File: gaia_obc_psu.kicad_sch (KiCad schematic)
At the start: 20 parts, among them J3 Conn_01x02_Pin, Q1 FS8205A, U2 LGS4056H, U3 DW01A, U5 AP2112K-3.3, U8 INA219AxDCN

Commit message: preparing ina3221
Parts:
- removed J3: Conn_01x02_Pin, Connector_Molex:Molex_MicroClasp_55935-0230_1x02_P2.00mm_Horizontal, symbol Connector:Conn_01x02_Pin
- removed U8: INA219AxDCN, Package_TO_SOT_SMD:SOT-23-8, symbol Sensor_Energy:INA219AxDCN
- added J4: Conn_01x02_Pin, Connector_Molex:Molex_MicroClasp_55935-0230_1x02_P2.00mm_Horizontal, symbol Connector:Conn_01x02_Pin
- added R13, R14, R15, R16, R17, R18: R_Small, symbol Device:R_Small
- added R19, R20, R21, R22: 10k, symbol Device:R_Small
- added U10, U9: INA3221, Package_DFN_QFN:Texas_RGV0016A_VQFN-16-1EP_4x4mm_P0.65mm_EP2.1x2.1mm, symbol Power_Management:INA3221
- added U11, U12, U8: AP2112K-3.3, Package_TO_SOT_SMD:SOT-23-5, symbol Regulator_Linear:AP2112K-3.3
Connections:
- net +BATT: now also J4.1 (Pin_1)
- net GND: now also U11.2 (GND), U12.2 (GND), U8.2 (GND), U9.17 (EP), U9.3 (GND)
- net VCC: now also J4.2 (Pin_2), R13.1, R14.1, R15.1, U9.1 (IN-3), U9.11 (IN-1), U9.14 (IN-2), U9.4 (VS), U9.5 (A0); no longer C9.1, U5.1 (VIN), U5.3 (EN)
- new net: R19.2, U9.9 (CRITICAL)
- new net: R22.2, U9.10 (PV)
- new net: R15.2, U9.12 (IN+1)
- new net: R21.2, U9.13 (TC)
- new net: R14.2, U9.15 (IN+2)
- new net: R22.1, U9.16 (VPU)
- new net: R13.2, U9.2 (IN+3)
- new net: R20.2, U9.8 (WARNING)
- new net: C9.1, U5.1 (VIN), U5.3 (EN)
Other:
- moved on the sheet: C7, C8, C9, U5

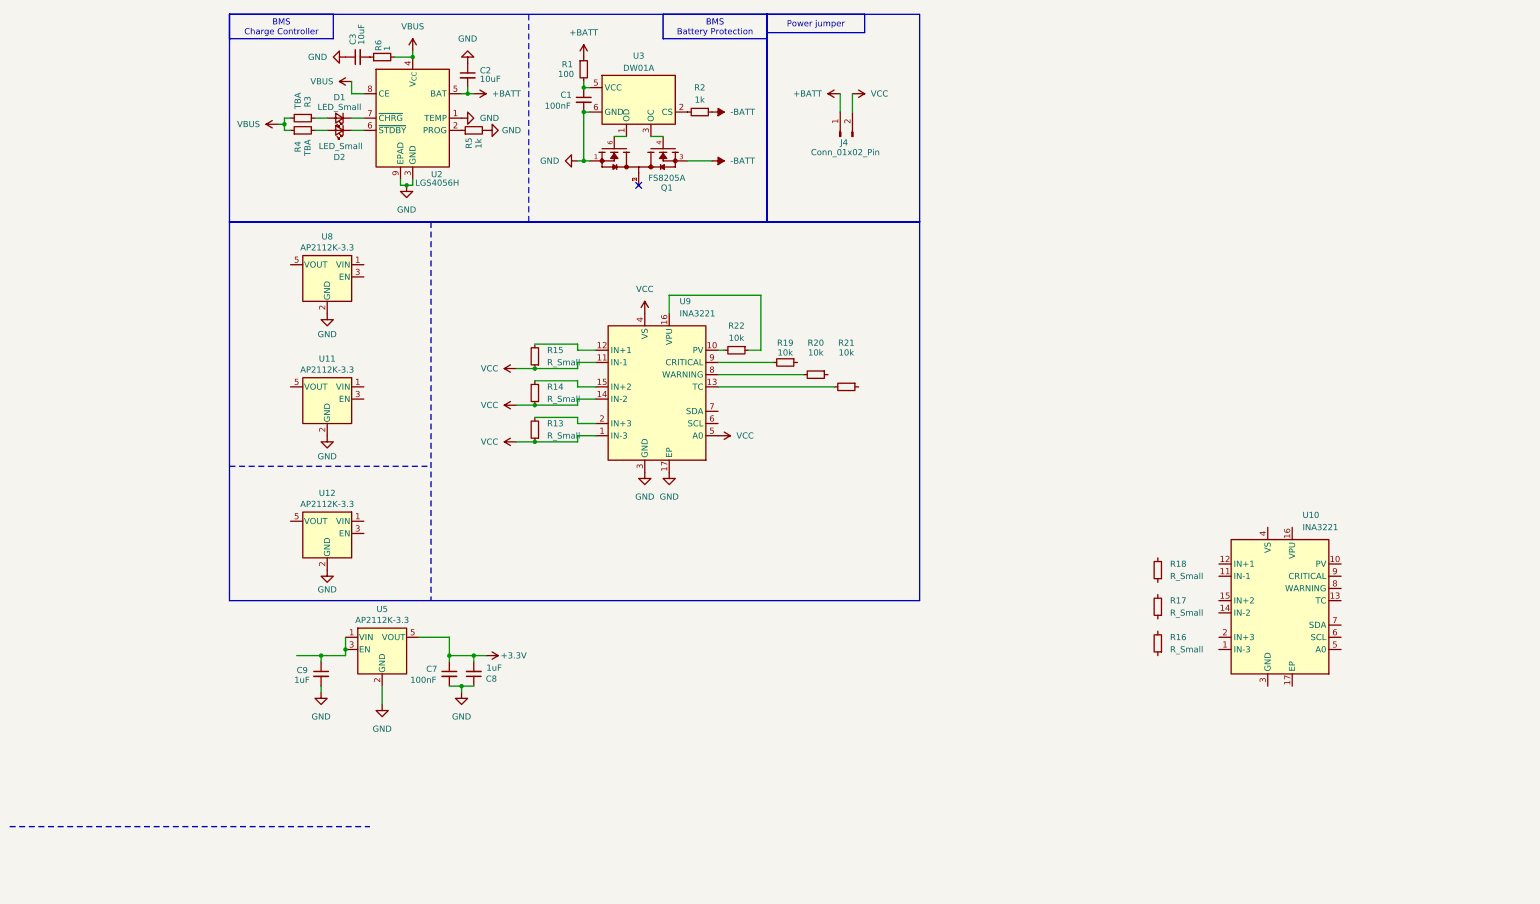
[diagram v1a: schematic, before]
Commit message: creating psu switches
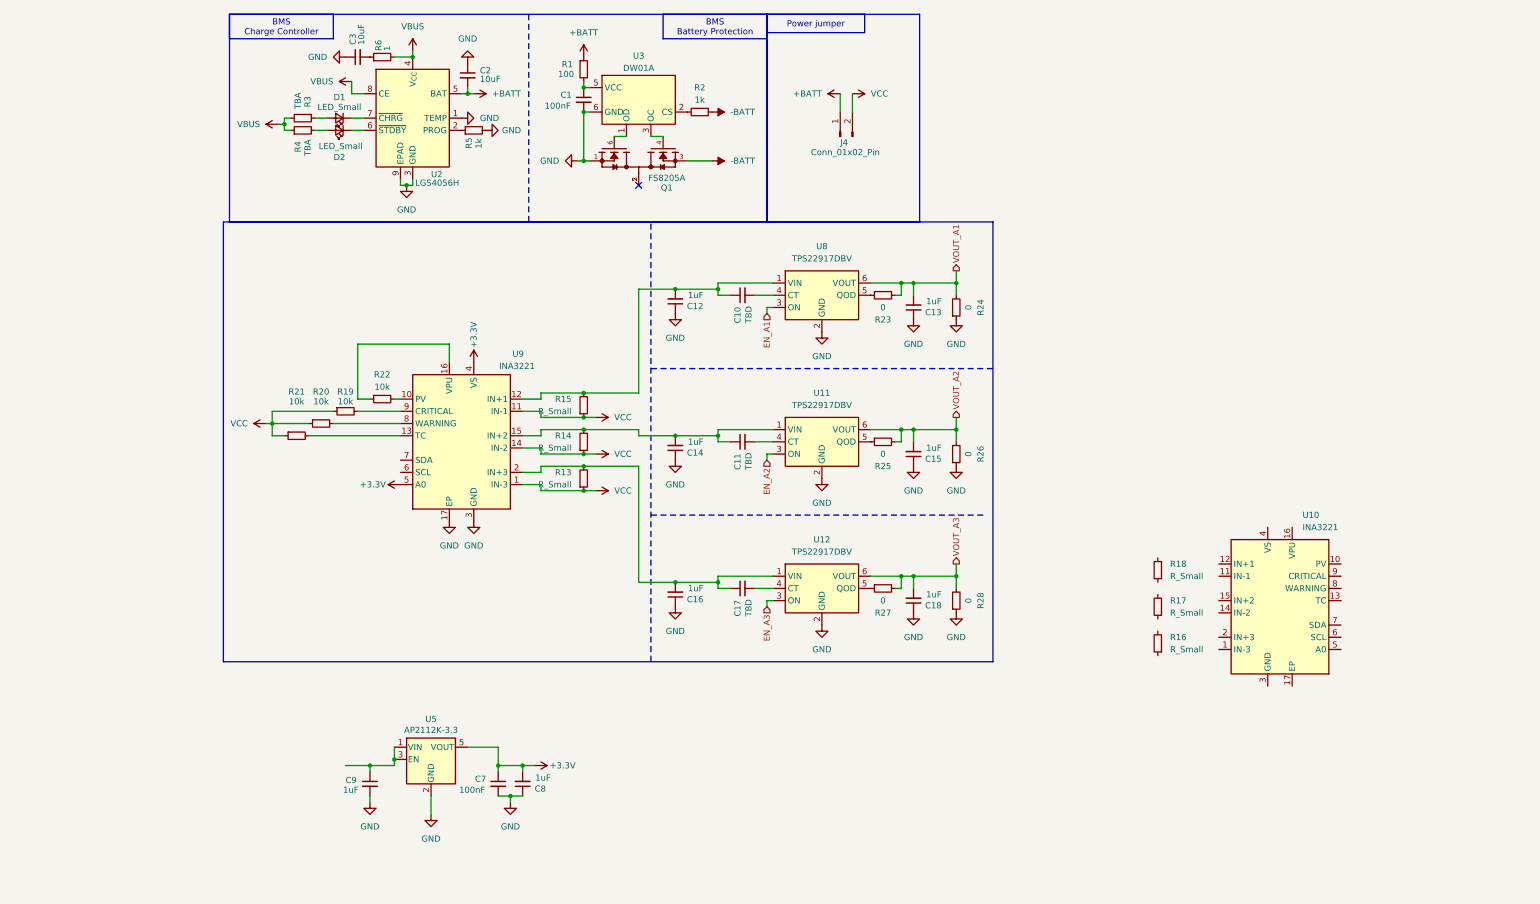
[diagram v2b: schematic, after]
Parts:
- removed U11, U12, U8: AP2112K-3.3, Package_TO_SOT_SMD:SOT-23-5, symbol Regulator_Linear:AP2112K-3.3
- added C10, C11, C17: TBD, symbol Device:C_Small
- added C12, C13, C14, C15, C16, C18: 1uF, symbol Device:C_Small
- added R23, R24, R25, R26, R27, R28: 0, symbol Device:R_Small
- added U11, U12, U8: TPS22917DBV, Package_TO_SOT_SMD:SOT-23-6, symbol Power_Management:TPS22917DBV
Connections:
- net +3.3V: now also U9.4 (VS), U9.5 (A0)
- net GND: now also C12.1, C13.1, C14.1, C15.1, C16.1, C18.1, R24.1, R26.1, R28.1, U11.2 (GND), U12.2 (GND), U8.2 (GND)
- net VCC: now also R19.1, R20.1, R21.1; no longer U9.4 (VS), U9.5 (A0)
- net at R15.2, U9.12 (IN+1): now also C10.1, C12.2, U8.1 (VIN)
- net at R14.2, U9.15 (IN+2): now also C11.1, C14.2, U11.1 (VIN)
- net at R13.2, U9.2 (IN+3): now also C16.2, C17.1, U12.1 (VIN)
- new net: C10.2, U8.4 (CT)
- new net: C11.2, U11.4 (CT)
- new net: R25.1, U11.5 (QOD)
- new net: R23.1, U8.5 (QOD)
- new net: C17.2, U12.4 (CT)
- new net: R27.1, U12.5 (QOD)
- new net EN_A1: U8.3 (ON)
- new net EN_A2: U11.3 (ON)
- new net EN_A3: U12.3 (ON)
- new net VOUT_A1: C13.2, R23.2, R24.2, U8.6 (VOUT)
- new net VOUT_A2: C15.2, R25.2, R26.2, U11.6 (VOUT)
- new net VOUT_A3: C18.2, R27.2, R28.2, U12.6 (VOUT)
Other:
- moved on the sheet: C7, C8, C9, R13, R14, R15, R19, R20, R21, R22, U5, U9

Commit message: finishing psu
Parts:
- removed R16, R17, R18: R_Small, symbol Device:R_Small
- removed U10: INA3221, Package_DFN_QFN:Texas_RGV0016A_VQFN-16-1EP_4x4mm_P0.65mm_EP2.1x2.1mm, symbol Power_Management:INA3221
- removed U2: LGS4056H, Package_DFN_QFN:DFN-8-1EP_3x3mm_P0.65mm_EP1.7x2.05mm, symbol OnionSAT_Gaia:LGS4056H
- added C19, C20, C25, C26: 1uF, symbol Device:C_Small
- added C22, C23: TBD, symbol Device:C_Small
- added R29, R30, R31, R32: 10k, symbol Device:R_Small
- added R33, R34, R35: R_Small, symbol Device:R_Small
- added R36, R37, R39, R40: 0, symbol Device:R_Small
- added U10: TP4056-42-ESOP8, Package_SO:SOIC-8-1EP_3.9x4.9mm_P1.27mm_EP2.41x3.3mm_ThermalVias, symbol Battery_Management:TP4056-42-ESOP8
- added U13: INA3221, Package_DFN_QFN:Texas_RGV0016A_VQFN-16-1EP_4x4mm_P0.65mm_EP2.1x2.1mm, symbol Power_Management:INA3221
- added U14, U15: TPS22917DBV, Package_TO_SOT_SMD:SOT-23-6, symbol Power_Management:TPS22917DBV
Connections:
- net +3.3V: now also R19.1, R20.1, R21.1, R29.1, R30.1, R31.1, U13.4 (VS), U13.5 (A0)
- net +BATT: now also U10.5 (BAT)
- net EN_A1: now also U14.3 (ON)
- net EN_A2: now also U15.3 (ON)
- net GND: now also C19.1, C20.1, C25.1, C26.1, R39.1, R40.1, U10.1 (TEMP), U10.3 (GND), U10.9 (EPAD), U13.17 (EP), U13.3 (GND), U14.2 (GND), U15.2 (GND)
- net VBUS: now also U10.4 (V_{CC}), U10.8 (CE)
- net VCC: now also R33.1, R34.1, R35.1, U13.1 (IN-3), U13.11 (IN-1), U13.14 (IN-2); no longer R19.1, R20.1, R21.1
- net VOUT_A1: now also C25.2, R36.2, R39.2, U14.6 (VOUT)
- net VOUT_A2: now also C26.2, R37.2, R40.2, U15.6 (VOUT)
- net at R5.1: now also U10.2 (PROG)
- net at D2.1 (K): now also U10.6 (~{STDBY})
- net at D1.1 (K): now also U10.7 (~{CHRG})
- net at C9.1, U5.1 (VIN), U5.3 (EN): now also R35.2, U13.2 (IN+3)
- new net: C19.2, C22.1, R33.2, U13.12 (IN+1), U14.1 (VIN)
- new net: R30.2, U13.8 (WARNING)
- new net: C20.2, C23.1, R34.2, U13.15 (IN+2), U15.1 (VIN)
- new net: C23.2, U15.4 (CT)
- new net: R37.1, U15.5 (QOD)
- new net: C22.2, U14.4 (CT)
- new net: R29.2, U13.13 (TC)
- new net: R32.2, U13.10 (PV)
- new net: R32.1, U13.16 (VPU)
- new net: R31.2, U13.9 (CRITICAL)
- new net: R36.1, U14.5 (QOD)
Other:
- moved on the sheet: C1, C10, C11, C12, C13, C14, C15, C16, C17, C18, C2, C3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

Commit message: almost final release
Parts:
- removed U10: TP4056-42-ESOP8, Package_SO:SOIC-8-1EP_3.9x4.9mm_P1.27mm_EP2.41x3.3mm_ThermalVias, symbol Battery_Management:TP4056-42-ESOP8
- added C32: 10uF, Capacitor_SMD:C_0402_1005Metric, symbol Device:C_Small
- added C33, C37: 1uF, Capacitor_SMD:C_0402_1005Metric, symbol Device:C_Small
- added C35: 100nF, Capacitor_SMD:C_0402_1005Metric, symbol Device:C_Small
- added IC1: MAX17048G+T10, gaia_obc-footprints:SON50P200X200X80-9N-D, symbol gaia_obc-symbols:MAX17048G+T10
- added R44, R45: 100k, symbol Device:R_Small
- added U13: AP2112K-3.0, Package_TO_SOT_SMD:SOT-23-5, symbol Regulator_Linear:AP2112K-3.3
- added U14: LGS4056HDB, Package_DFN_QFN:DFN-8-1EP_3x3mm_P0.65mm_EP1.55x2.4mm, symbol gaia_obc-symbols:LGS4056HDB
- C13: renamed from C12; footprint (none) -> Capacitor_SMD:C_0402_1005Metric
- C14: footprint (none) -> Capacitor_SMD:C_0402_1005Metric
- C15: renamed from C16; footprint (none) -> Capacitor_SMD:C_0402_1005Metric
- C16: renamed from C19; footprint (none) -> Capacitor_SMD:C_0402_1005Metric
- C17: renamed from C20; footprint (none) -> Capacitor_SMD:C_0402_1005Metric
- C18: renamed from C10; value TBD -> 1nF
- C19: renamed from C11; value TBD -> 1nF
- C20: renamed from C17; value TBD -> 1nF
- C21: renamed from C22; value TBD -> 1nF
- C22: renamed from C23; value TBD -> 1nF
- C23: renamed from C9; footprint (none) -> Capacitor_SMD:C_0402_1005Metric
- C24: renamed from C7; footprint (none) -> Capacitor_SMD:C_0402_1005Metric
- C25: renamed from C8; footprint (none) -> Capacitor_SMD:C_0402_1005Metric
- C26: renamed from C13; footprint (none) -> Capacitor_SMD:C_0402_1005Metric
- C27: renamed from C15; footprint (none) -> Capacitor_SMD:C_0402_1005Metric
- C28: renamed from C18; footprint (none) -> Capacitor_SMD:C_0402_1005Metric
- C29: renamed from C25; footprint (none) -> Capacitor_SMD:C_0402_1005Metric
- C30: renamed from C26; footprint (none) -> Capacitor_SMD:C_0402_1005Metric
- C31: renamed from C1; footprint (none) -> Capacitor_SMD:C_0402_1005Metric
- C34: renamed from C3; footprint (none) -> Capacitor_SMD:C_0402_1005Metric
- C36: renamed from C2; footprint (none) -> Capacitor_SMD:C_0402_1005Metric
- renumbered R21 to R14, R29 to R15, R20 to R16, R30 to R17, R19 to R18, R31 to R19, R22 to R20, R32 to R21, R15 to R22, R14 to R23, R13 to R24, R33 to R25, R34 to R26, R35 to R27, R23 to R28, R25 to R29, R27 to R30, R36 to R31, R37 to R32, R24 to R33, R26 to R34, R28 to R35, R39 to R36, R40 to R37, R1 to R38, R3 to R39, R4 to R40, R2 to R41, R6 to R42, R5 to R43, U15 to U10, U5 to U11, U3 to U12, U9 to U4, U13 to U5, U8 to U6, U11 to U7, U12 to U8, U14 to U9
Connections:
- net +3.3V: no longer C24.1, C25.2, U11.5 (VOUT), U4.5 (A0)
- net +BATT: now also C32.2, IC1.2 (CELL), IC1.3 (VDD), R45.2, U14.5 (BAT)
- net EN_A1: no longer U9.3 (ON)
- net EN_A2: no longer U10.3 (ON)
- net GND: now also U4.5 (A0), C32.1, C33.2, C35.2, C37.1, IC1.1 (CTG), IC1.4 (GND), IC1.9 (EP), R44.1, U13.2 (GND), U14.1 (TEMP), U14.3 (GND), U14.9 (EPAD)
- net VBUS: now also U14.4 (V_{CC}), U14.8 (CE)
- net VOUT_A1: no longer C29.2, R31.2, R36.2, U9.6 (VOUT)
- net VOUT_A2: no longer C30.2, R32.2, R37.2, U10.6 (VOUT)
- net I2C_1_SCL: now reaches U4.6 (SCL)
- net I2C_1_SCL: now also U5.6 (SCL), IC1.7 (SCL)
- net I2C_1_SDA: now reaches U4.7 (SDA)
- net I2C_1_SDA: now also U5.7 (SDA), IC1.8 (SDA)
- net at R43.1: now also U14.2 (PROG)
- net at D2.1 (K): now also U14.6 (~{STDBY})
- net at D1.1 (K): now also U14.7 (~{CHRG})
- net OBC_BATT: now reaches C23.1, R27.2, U11.1 (VIN), U11.3 (EN), U5.2 (IN+3)
- net OBC_BATT: now also C33.1, U13.1 (VIN), U13.3 (EN)
- new net: IC1.6 (QSTRT), R44.2
- new net: IC1.5 (~{ALRT}), R45.1
- new net EN_B1: U9.3 (ON)
- new net EN_B2: U10.3 (ON)
- new net OBC_3V0: C35.1, C37.2, U13.5 (VOUT)
- new net OBC_3V3: C24.1, C25.2, U11.5 (VOUT)
- new net VOUT_B1: C29.2, R31.2, R36.2, U9.6 (VOUT)
- new net VOUT_B2: C30.2, R32.2, R37.2, U10.6 (VOUT)
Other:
- moved on the sheet: C31, Q1, R38, R41, U12

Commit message: prep for routing 2/1
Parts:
- C18, C19, C20, C21, C22: footprint (none) -> Capacitor_SMD:C_0402_1005Metric
- D1, D2: footprint (none) -> LED_SMD:LED_0603_1608Metric
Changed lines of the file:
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@@
 			)
 		)
-		(property "Footprint" ""
+		(property "Footprint" "Capacitor_SMD:C_0402_1005Metric"
 			(at 120.65 29.21 0)
 			(effects
@@
 			)
 		)
-		(property "Footprint" ""
+		(property "Footprint" "Capacitor_SMD:C_0402_1005Metric"
 			(at 120.65 120.65 0)
 			(effects
@@
 			)
 		)
-		(property "Footprint" ""
+		(property "Footprint" "Capacitor_SMD:C_0402_1005Metric"
 			(at 120.65 151.13 0)
 			(effects
@@
 			)
 		)
-		(property "Footprint" ""
+		(property "Footprint" "LED_SMD:LED_0603_1608Metric"
 			(at 219.71 39.37 90)
 			(effects
@@
 			)
 		)
-		(property "Footprint" ""
+		(property "Footprint" "Capacitor_SMD:C_0402_1005Metric"
 			(at 120.65 90.17 0)
 			(effects
@@
 			)
 		)
-		(property "Footprint" ""
+		(property "Footprint" "LED_SMD:LED_0603_1608Metric"
 			(at 219.71 36.83 90)
 			(effects
@@
 			)
 		)
-		(property "Footprint" ""
+		(property "Footprint" "Capacitor_SMD:C_0402_1005Metric"
 			(at 120.65 59.69 0)
 			(effects

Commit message: almost routeable//98% done schema
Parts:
- R23: renamed from R14; footprint (none) -> Resistor_SMD:R_0402_1005Metric
- R24: renamed from R15; footprint (none) -> Resistor_SMD:R_0402_1005Metric
- R25: renamed from R16; footprint (none) -> Resistor_SMD:R_0402_1005Metric
- R26: renamed from R17; footprint (none) -> Resistor_SMD:R_0402_1005Metric
- R27: renamed from R18; footprint (none) -> Resistor_SMD:R_0402_1005Metric
- R28: renamed from R19; footprint (none) -> Resistor_SMD:R_0402_1005Metric
- R29: renamed from R20; footprint (none) -> Resistor_SMD:R_0402_1005Metric
- R30: renamed from R21; footprint (none) -> Resistor_SMD:R_0402_1005Metric
- R31: renamed from R22; footprint (none) -> Resistor_SMD:R_0603_1608Metric
- R32: renamed from R23; footprint (none) -> Resistor_SMD:R_0603_1608Metric
- R33: renamed from R24; footprint (none) -> Resistor_SMD:R_0603_1608Metric
- R34: renamed from R25; footprint (none) -> Resistor_SMD:R_0603_1608Metric
- R35: renamed from R26; footprint (none) -> Resistor_SMD:R_0603_1608Metric
- R36: renamed from R27; footprint (none) -> Resistor_SMD:R_0603_1608Metric
- R37: renamed from R28; footprint (none) -> Resistor_SMD:R_0402_1005Metric
- R38: renamed from R29; footprint (none) -> Resistor_SMD:R_0402_1005Metric
- R39: renamed from R30; footprint (none) -> Resistor_SMD:R_0402_1005Metric
- R40: renamed from R31; footprint (none) -> Resistor_SMD:R_0402_1005Metric
- R41: renamed from R32; footprint (none) -> Resistor_SMD:R_0402_1005Metric
- R42: renamed from R33; footprint (none) -> Resistor_SMD:R_0402_1005Metric
- R43: renamed from R34; footprint (none) -> Resistor_SMD:R_0402_1005Metric
- R44: renamed from R35; footprint (none) -> Resistor_SMD:R_0402_1005Metric
- R45: renamed from R36; footprint (none) -> Resistor_SMD:R_0402_1005Metric
- R46: renamed from R37; footprint (none) -> Resistor_SMD:R_0402_1005Metric
- R47: renamed from R38; footprint (none) -> Resistor_SMD:R_1206_3216Metric
- R48: renamed from R39; footprint (none) -> Resistor_SMD:R_0402_1005Metric
- R49: renamed from R40; footprint (none) -> Resistor_SMD:R_0402_1005Metric
- R50: renamed from R41; footprint (none) -> Resistor_SMD:R_0603_1608Metric
- R51: renamed from R42; footprint (none) -> Resistor_SMD:R_0603_1608Metric
- R52: renamed from R43; footprint (none) -> Resistor_SMD:R_0603_1608Metric
- R53: renamed from R44; footprint (none) -> Resistor_SMD:R_0603_1608Metric
- R54: renamed from R45; footprint (none) -> Resistor_SMD:R_0603_1608Metric
- renumbered D1 to D10, D2 to D11

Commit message: ready for approval
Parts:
- R31, R32, R33, R34, R35, R36: value R_Small -> 0,1
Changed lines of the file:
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@@
 		)
 	)
-	(text_box "OBC Power"
+	(text_box "A2 Power"
 		(exclude_from_sim no)
 		(at 154.94 72.39 0)
@@
 		)
 	)
-	(text_box "OBC Power"
+	(text_box "A1 Power"
 		(exclude_from_sim no)
 		(at 154.94 41.91 0)
@@
 		)
 	)
-	(text_box "OBC Power"
+	(text_box "B1 Power"
 		(exclude_from_sim no)
 		(at 154.94 133.35 0)
@@
 		)
 	)
-	(text_box "OBC Power"
+	(text_box "B2 Power"
 		(exclude_from_sim no)
 		(at 154.94 163.83 0)
@@
 		)
 	)
-	(text_box "OBC Power"
+	(text_box "A3 Power"
 		(exclude_from_sim no)
 		(at 154.94 102.87 0)
@@
 			)
 		)
-		(property "Value" "R_Small"
+		(property "Value" "0,1"
 			(at 85.09 144.7799 0)
 			(effects
@@
 			)
 		)
-		(property "Value" "R_Small"
+		(property "Value" "0,1"
 			(at 85.09 53.3399 0)
 			(effects
@@
 			)
 		)
-		(property "Value" "R_Small"
+		(property "Value" "0,1"
 			(at 85.09 152.3999 0)
 			(effects
@@
 			)
 		)
-		(property "Value" "R_Small"
+		(property "Value" "0,1"
 			(at 85.09 60.9599 0)
 			(effects
@@
 			)
 		)
-		(property "Value" "R_Small"
+		(property "Value" "0,1"
 			(at 85.09 160.0199 0)
 			(effects
@@
 			)
 		)
-		(property "Value" "R_Small"
+		(property "Value" "0,1"
 			(at 85.09 68.5799 0)
 			(effects
